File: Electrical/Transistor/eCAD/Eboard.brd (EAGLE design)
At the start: 71.3 x 54.1 mm, 22 parts

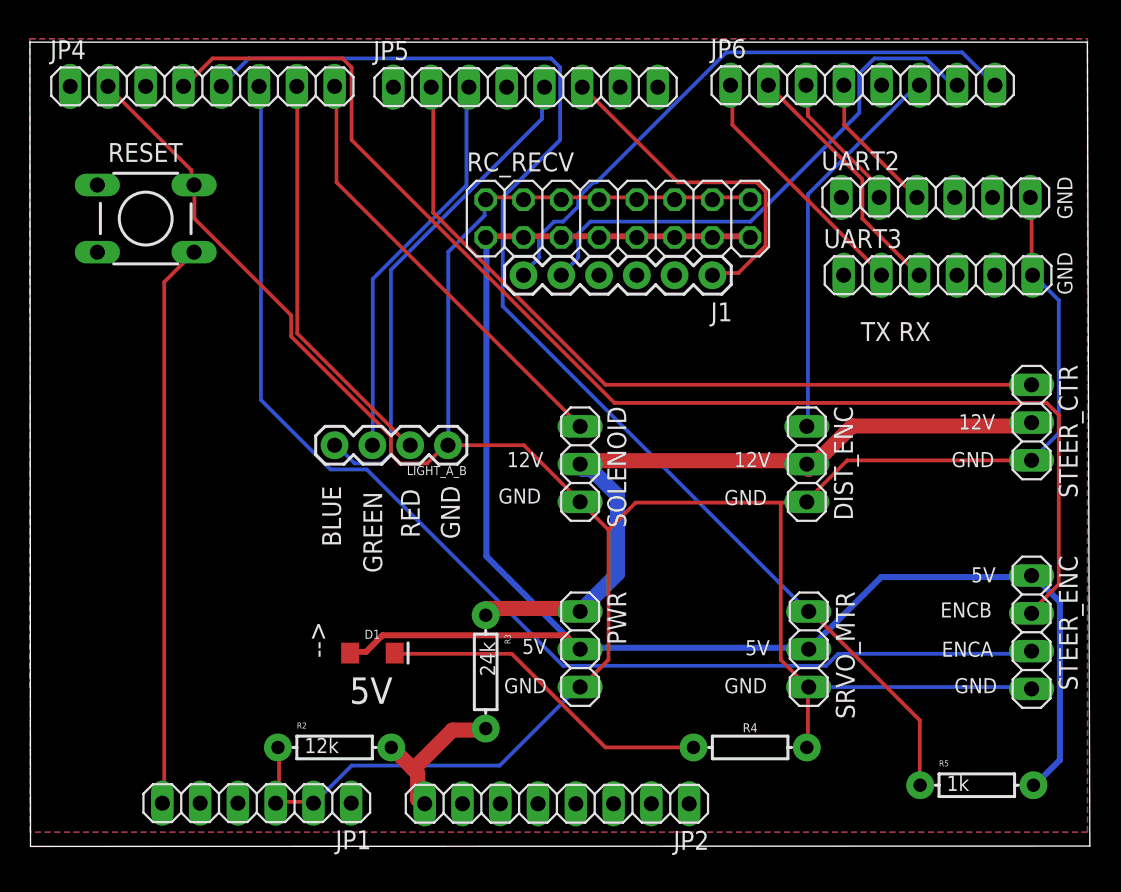
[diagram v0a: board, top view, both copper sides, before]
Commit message: added 12V silkscreen, changed servo mtr to two-pin connector, rerouted accordingly
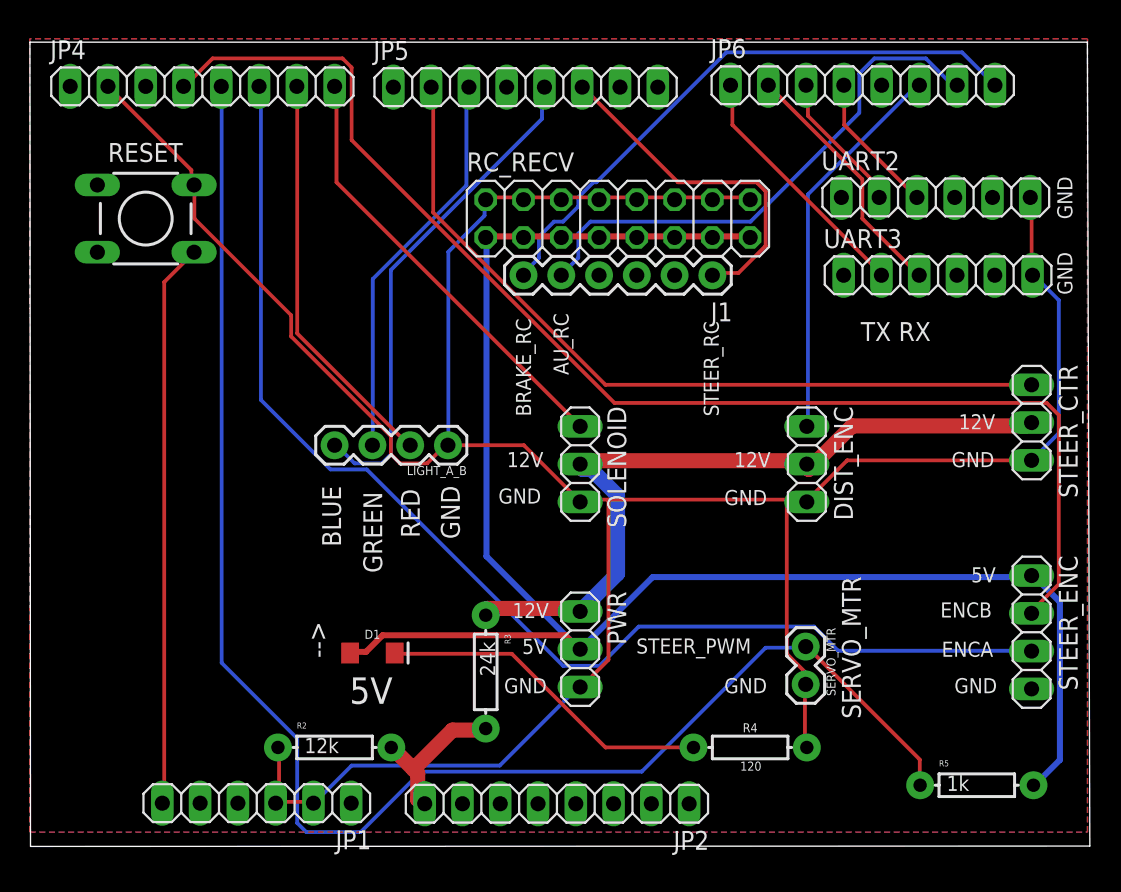
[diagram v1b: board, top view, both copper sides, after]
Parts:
- removed SRVO_MTR: (no value), pinhead:1X03
- added SERVO_MTR: (no value), SparkFun-Connectors:1X02
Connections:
- new net N$3: STEER_ENC.4
- net 5V: no longer SRVO_MTR.2
- net GND: now also SERVO_MTR.2; no longer SRVO_MTR.3, STEER_ENC.4
- net SRVO_MTR: now also SERVO_MTR.1; no longer SRVO_MTR.1
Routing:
- net SRVO_MTR: track 85.4 -> 103.8 mm
- net GND: track 208.3 -> 195.2 mm
- net STEER_ENCA: track 80.9 -> 82.1 mm
- added copper zone on layer 16, net N$4
- removed copper zone on layer 16, net N$3
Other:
- board text added: "120"
- board text added: "AU_RC"
- board text added: "BRAKE_RC"
- board text added: "SERVO_MTR"
- board text added: "STEER_PWM"
- board text added: "STEER_RC"

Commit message: modified distances between pins so that they will align with the mega, then modified back silkscreen to robobuggy rev 1.8.1
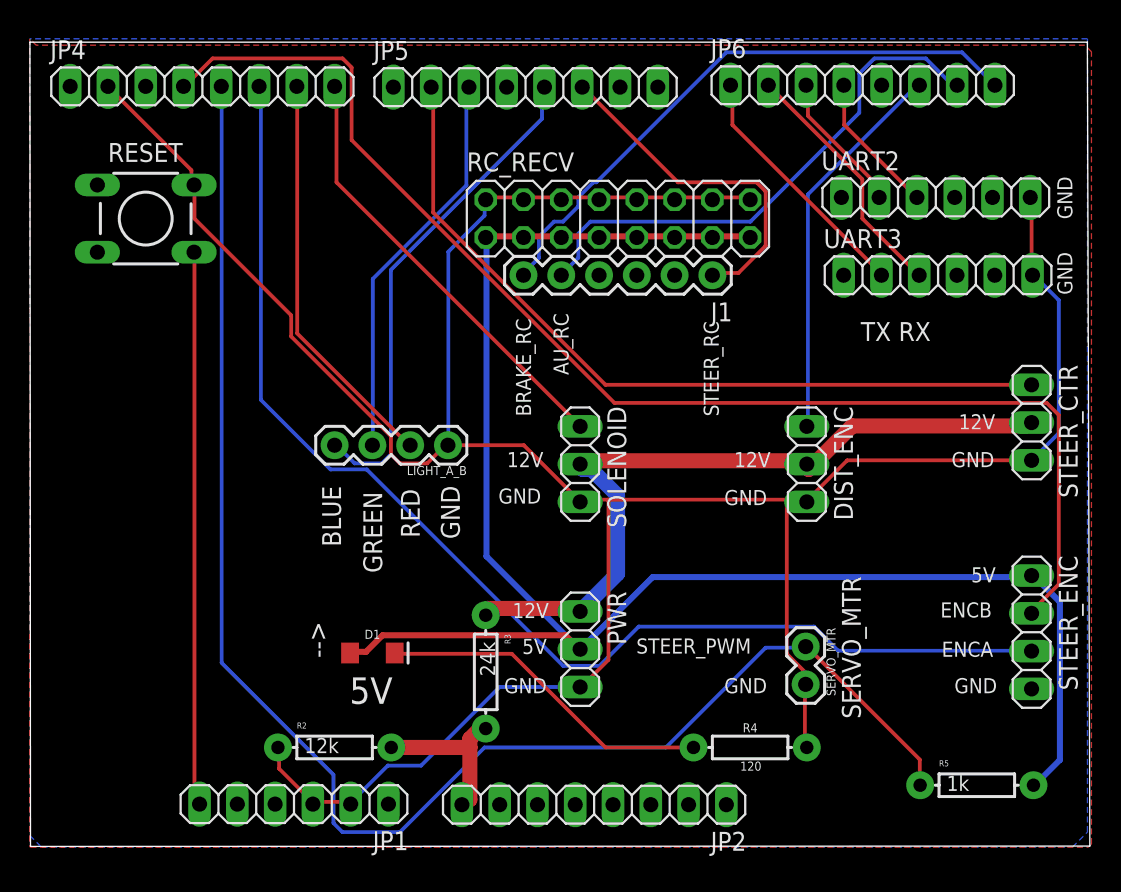
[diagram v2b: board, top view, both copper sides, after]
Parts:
- moved JP1 2.50 mm to (20.3, 47.6)
- moved JP2 2.50 mm to (40.5, 47.6)
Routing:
- net GND: track 195.2 -> 193.6 mm
- net SRVO_MTR: track 103.8 -> 102.4 mm
- net SWITCH: track 37.9 -> 37.2 mm
- net VBATT_ADC: track 10.8 -> 11.3 mm
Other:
- board text added: "ROBOBUGGY REV 1.8.1"
- board text removed: "ROBOBUGGY REV 1.8"

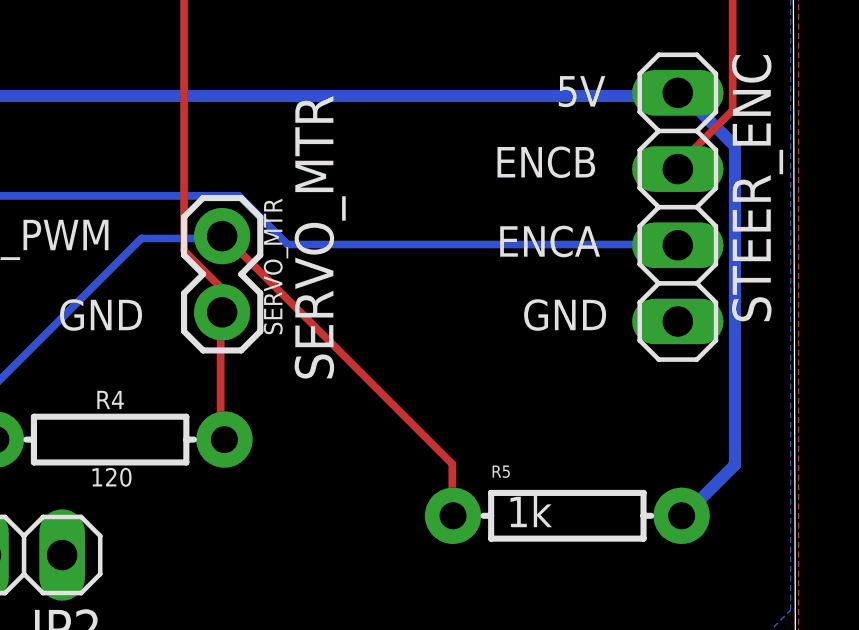
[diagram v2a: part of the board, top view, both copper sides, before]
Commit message: added gnd pin to encoders
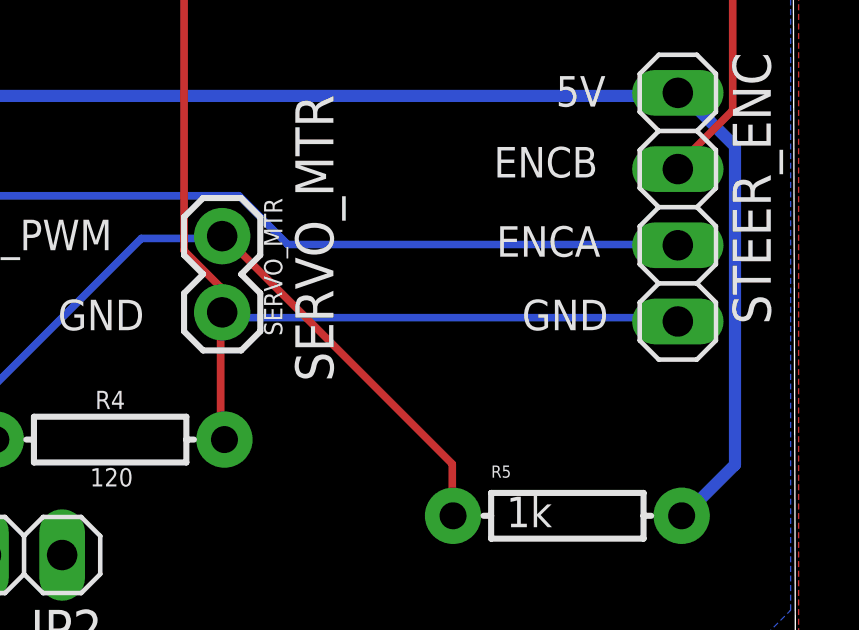
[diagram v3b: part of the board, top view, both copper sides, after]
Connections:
- removed net N$3: STEER_ENC.4
- net GND: now also STEER_ENC.4
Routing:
- net GND: track 193.6 -> 209.0 mm
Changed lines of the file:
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@@
 <wire x1="39.5478" y1="55.4736" x2="34.1376" y2="55.4736" width="0.254" layer="16"/>
 <wire x1="24.1808" y1="47.752" x2="24.1173" y2="47.5996" width="0.254" layer="16"/>
+<contactref element="STEER_ENC" pad="4"/>
+<wire x1="54.864" y1="55.4736" x2="69.9008" y2="55.4736" width="0.254" layer="16"/>
+<wire x1="69.9008" y1="55.4736" x2="69.9008" y2="55.3466" width="0.254" layer="16"/>
+<wire x1="54.864" y1="55.4736" x2="54.7116" y2="55.6514" width="0.254" layer="16"/>
 </signal>
 <signal name="12V">
@@
 <wire x1="27.2288" y1="57.7088" x2="27.0778" y2="57.7596" width="0.254" layer="1"/>
 </signal>
-<signal name="N$3">
-<contactref element="STEER_ENC" pad="4"/>
-<wire x1="69.9008" y1="55.4736" x2="69.9008" y2="55.3466" width="0.254" layer="16"/>
-</signal>
 <signal name="N$2">
